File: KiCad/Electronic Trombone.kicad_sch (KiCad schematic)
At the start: 12 parts, among them J1 691137710002, U2 TL074, U3 TL074

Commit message: routed the filter, updated 0201 footprints to 0402
JLCPCB's economy PCBA has a footprint bottom limit of 0402 imperial
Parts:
- R10, R8: footprint Resistor_SMD:R_0201_0603Metric -> Resistor_SMD:R_0402_1005Metric
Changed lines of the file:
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@@
 			)
 		)
-		(property "Footprint" "Resistor_SMD:R_0201_0603Metric"
+		(property "Footprint" "Resistor_SMD:R_0402_1005Metric"
 			(at 131.064 136.144 90)
 			(hide yes)
@@
 			)
 		)
-		(property "Footprint" "Resistor_SMD:R_0201_0603Metric"
+		(property "Footprint" "Resistor_SMD:R_0402_1005Metric"
 			(at 145.034 123.444 90)
 			(hide yes)

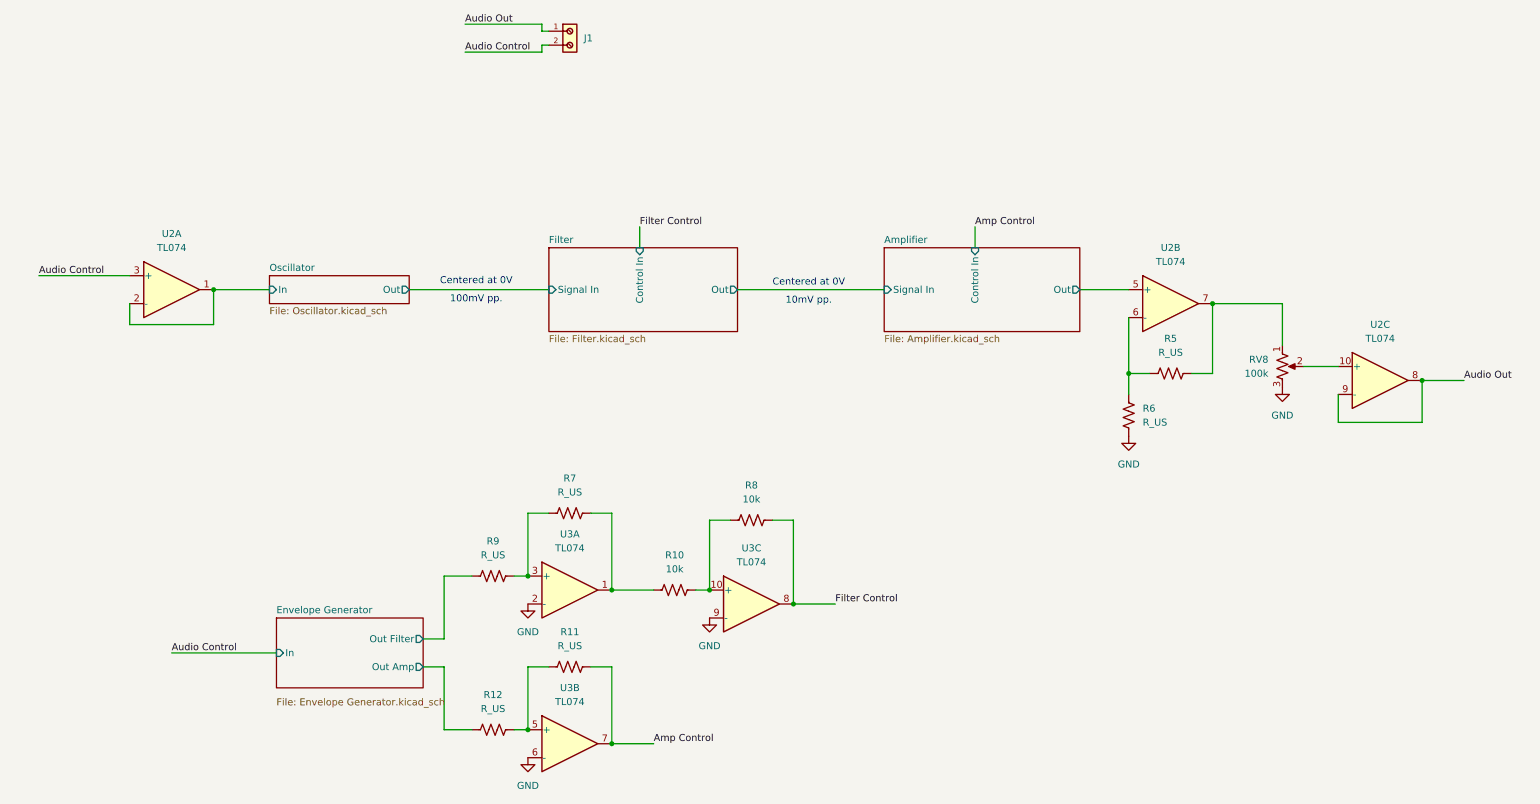
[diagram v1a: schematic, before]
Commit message: amplifier layout and routing
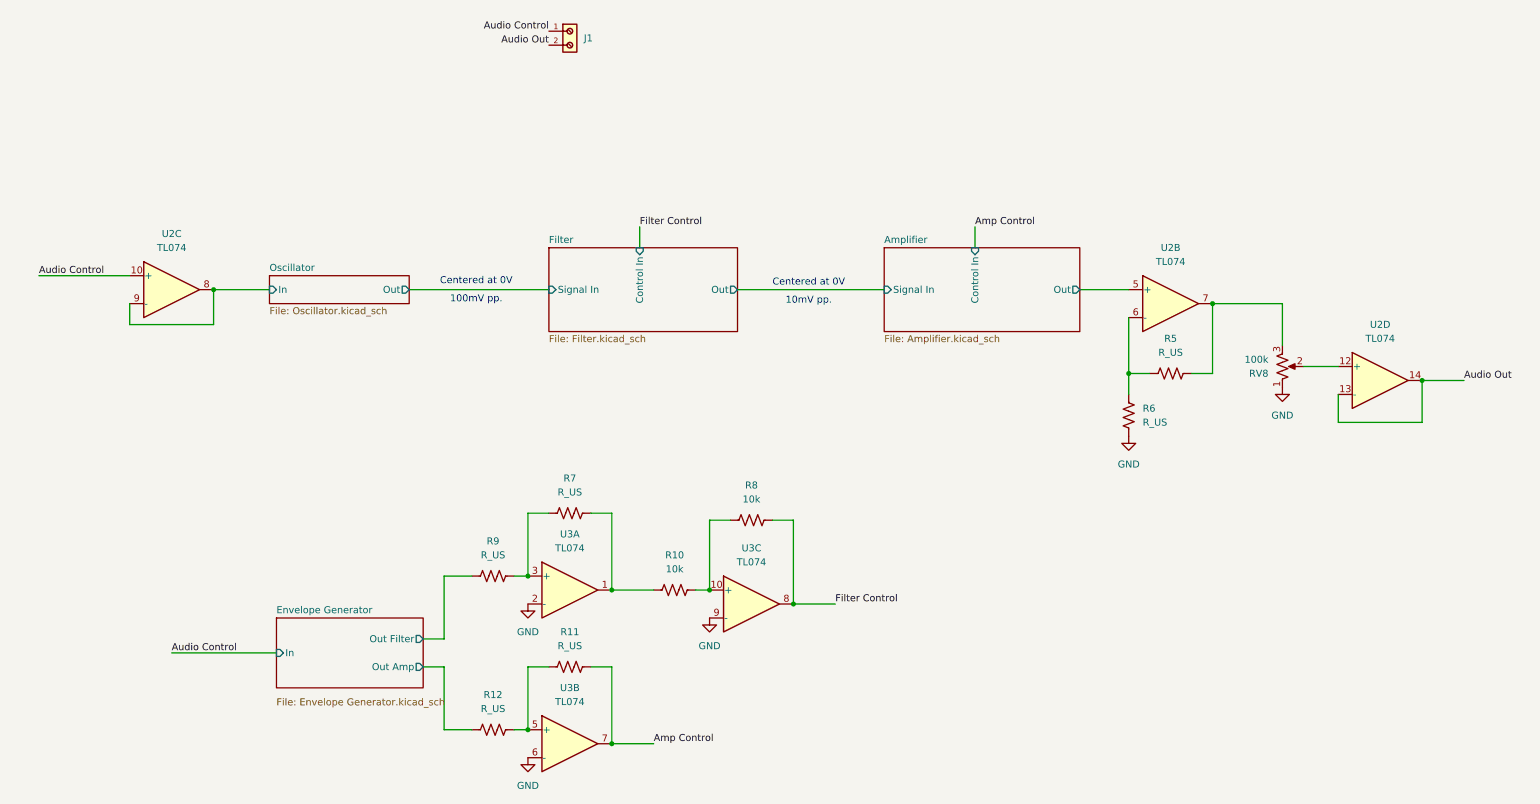
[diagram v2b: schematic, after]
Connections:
- net Audio Control: now also J1.1, U2.10 (+); no longer J1.2, U2.3 (+)
- net Audio Out: now also J1.2, U2.13 (-), U2.14; no longer J1.1, U2.8, U2.9 (-)
- net GND: now also RV8.1; no longer RV8.3
- net Oscillator/In: now also U2.8, U2.9 (-); no longer U2.1, U2.2 (-)
- net at RV8.2: now also U2.12 (+); no longer U2.10 (+)
- net at R5.2, U2.7: now also RV8.3; no longer RV8.1
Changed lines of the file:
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@@
-	(wire
-		(pts
-			(xy 92.71 34.29) (xy 106.68 34.29)
-		)
-		(stroke
-			(width 0)
-			(type default)
-		)
-	)
 	(wire
 		(pts
@@
 	(wire
 		(pts
-			(xy 92.71 39.37) (xy 106.68 39.37)
-		)
-		(stroke
-			(width 0)
-			(type default)
-		)
-	)
-	(wire
-		(pts
 			(xy 217.17 97.79) (xy 213.36 97.79)
 		)
@@
 	(wire
 		(pts
-			(xy 106.68 39.37) (xy 106.68 38.1)
-		)
-		(stroke
-			(width 0)
-			(type default)
-		)
-	)
-	(wire
-		(pts
 			(xy 46.99 88.9) (xy 46.99 82.55)
 		)
@@
 	(wire
 		(pts
-			(xy 106.68 38.1) (xy 107.95 38.1)
-		)
-		(stroke
-			(width 0)
-			(type default)
-		)
-	)
-	(wire
-		(pts
 			(xy 124.46 71.12) (xy 124.46 74.93)
 		)
@@
 	(wire
 		(pts
-			(xy 106.68 34.29) (xy 106.68 35.56)
-		)
-		(stroke
-			(width 0)
-			(type default)
-		)
-	)
-	(wire
-		(pts
 			(xy 107.95 151.13) (xy 104.14 151.13)
 		)
@@
 			(width 0)
 			(type default)
-		)
-	)
-	(wire
-		(pts
-			(xy 106.68 35.56) (xy 107.95 35.56)
-		)
-		(stroke
-			(width 0)
-			(type default)
-		)
-	)
-	(label "Audio Control"
-		(at 92.71 39.37 0)
-		(effects
-			(font
-				(size 1.27 1.27)
-			)
-			(justify left bottom)
 		)
 	)
@@
 	)
 	(label "Audio Out"
-		(at 92.71 34.29 0)
+		(at 107.95 38.1 180)
 		(effects
 			(font
 				(size 1.27 1.27)
 			)
-			(justify left bottom)
+			(justify right bottom)
 		)
 	)
@@
 			)
 			(justify left bottom)
+		)
+	)
+	(label "Audio Control"
+		(at 107.95 35.56 180)
+		(effects
+			(font
+				(size 1.27 1.27)
+			)
+			(justify right bottom)
 		)
 	)
@@
 		(lib_id "Amplifier_Operational:TL074")
 		(at 259.08 99.06 0)
-		(unit 3)
+		(unit 4)
 		(body_style 1)
 		(exclude_from_sim no)
@@
 				(path "/931827f3-33b7-460f-8885-7db258da2648"
 					(reference "U2")
-					(unit 3)
+					(unit 4)
 				)
 			)
@@
 		(lib_id "Device:R_Potentiometer_US")
 		(at 241.3 96.52 0)
+		(mirror x)
 		(unit 1)
 		(body_style 1)
@@
 		(in_pos_files yes)
 		(dnp no)
-		(fields_autoplaced yes)
 		(property "Reference" "RV8"
-			(at 238.76 95.2499 0)
+			(at 238.76 97.7901 0)
 			(show_name no)
 			(do_not_autoplace no)
@@
 		)
 		(property "Value" "100k"
-			(at 238.76 97.7899 0)
+			(at 238.76 95.2501 0)
 			(show_name no)
 			(do_not_autoplace no)
@@
 		(lib_id "Amplifier_Operational:TL074")
 		(at 39.37 82.55 0)
-		(unit 1)
+		(unit 3)
 		(body_style 1)
 		(exclude_from_sim no)
@@
 				(path "/931827f3-33b7-460f-8885-7db258da2648"
 					(reference "U2")
-					(unit 1)
-				)
-			)
+					(unit 3)
+				)
+			)

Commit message: placed and routed envelope core
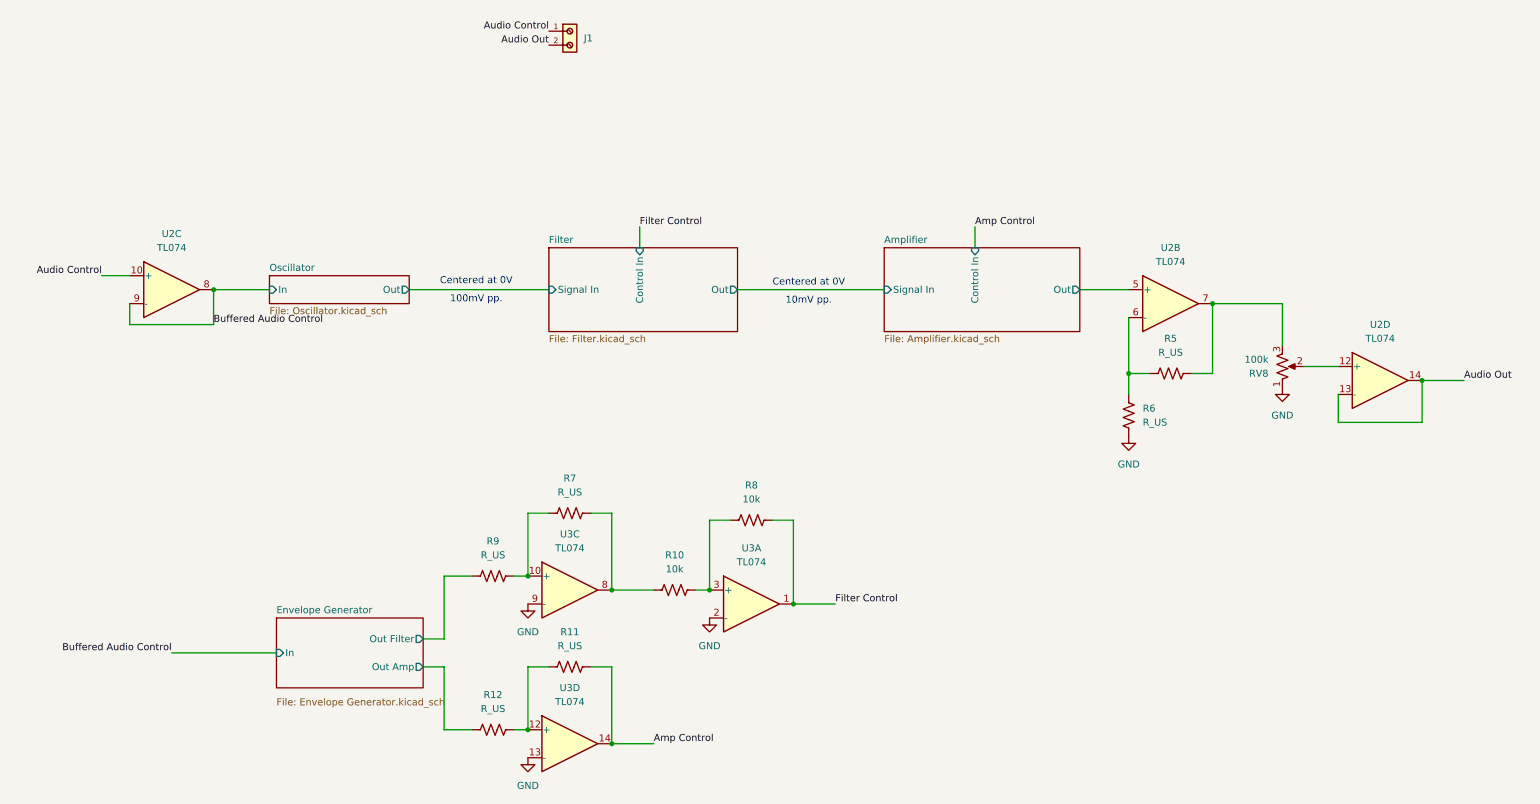
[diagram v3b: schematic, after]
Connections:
- net Amp Control: now also U3.14; no longer U3.7
- net Filter Control: now also U3.1; no longer U3.8
- net GND: now also U3.13 (-), U3.2 (-), U3.9 (-); no longer U3.2 (-), U3.6 (-), U3.9 (-)
- net at R10.2, R8.1: now also U3.3 (+); no longer U3.10 (+)
- net at R10.1, R7.2: now also U3.8; no longer U3.1
- net at R7.1, R9.2: now also U3.10 (+); no longer U3.3 (+)
- net at R11.1, R12.2: now also U3.12 (+); no longer U3.5 (+)
- net Oscillator/In renamed Buffered Audio Control
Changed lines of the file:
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@@
-	(wire
-		(pts
-			(xy 15.24 80.01) (xy 31.75 80.01)
-		)
-		(stroke
-			(width 0)
-			(type default)
-		)
-	)
 	(wire
 		(pts
@@
 	(wire
 		(pts
+			(xy 213.36 82.55) (xy 204.47 82.55)
+		)
+		(stroke
+			(width 0)
+			(type default)
+		)
+	)
+	(wire
+		(pts
+			(xy 115.57 123.19) (xy 119.38 123.19)
+		)
+		(stroke
+			(width 0)
+			(type default)
+		)
+	)
+	(wire
+		(pts
 			(xy 39.37 148.59) (xy 58.42 148.59)
 		)
@@
 	(wire
 		(pts
-			(xy 213.36 82.55) (xy 204.47 82.55)
-		)
-		(stroke
-			(width 0)
-			(type default)
-		)
-	)
-	(wire
-		(pts
-			(xy 115.57 123.19) (xy 119.38 123.19)
-		)
-		(stroke
-			(width 0)
-			(type default)
-		)
-	)
-	(wire
-		(pts
 			(xy 46.99 82.55) (xy 57.15 82.55)
 		)
@@
 	(wire
 		(pts
+			(xy 26.67 80.01) (xy 31.75 80.01)
+		)
+		(stroke
+			(width 0)
+			(type default)
+		)
+	)
+	(wire
+		(pts
 			(xy 241.3 92.71) (xy 241.3 85.09)
 		)
@@
 		)
 	)
-	(label "Audio Control"
-		(at 15.24 80.01 0)
+	(label "Buffered Audio Control"
+		(at 46.99 88.9 0)
 		(effects
 			(font
@@
 			)
 			(justify left bottom)
+		)
+	)
+	(label "Audio Control"
+		(at 26.67 80.01 180)
+		(effects
+			(font
+				(size 1.27 1.27)
+			)
+			(justify right bottom)
 		)
 	)
@@
 		)
 	)
-	(label "Audio Control"
-		(at 39.37 148.59 0)
-		(effects
-			(font
-				(size 1.27 1.27)
-			)
-			(justify left bottom)
-		)
-	)
 	(label "Amp Control"
 		(at 127 165.1 0)
@@
 		)
 	)
+	(label "Buffered Audio Control"
+		(at 39.37 148.59 180)
+		(effects
+			(font
+				(size 1.27 1.27)
+			)
+			(justify right bottom)
+		)
+	)
 	(label "Audio Out"
 		(at 274.32 99.06 0)
@@
 		(lib_id "Amplifier_Operational:TL074")
 		(at 144.78 139.7 0)
-		(unit 3)
+		(unit 1)
 		(body_style 1)
 		(exclude_from_sim no)
@@
 				(path "/931827f3-33b7-460f-8885-7db258da2648"
 					(reference "U3")
-					(unit 3)
+					(unit 1)
 				)
 			)
@@
 		(lib_id "Amplifier_Operational:TL074")
 		(at 111.76 137.16 0)
-		(unit 1)
+		(unit 3)
 		(body_style 1)
 		(exclude_from_sim no)
@@
 				(path "/931827f3-33b7-460f-8885-7db258da2648"
 					(reference "U3")
-					(unit 1)
+					(unit 3)
 				)
 			)
@@
 		(lib_id "Amplifier_Operational:TL074")
 		(at 111.76 165.1 0)
-		(unit 2)
+		(unit 4)
 		(body_style 1)
 		(exclude_from_sim no)
@@
 				(path "/931827f3-33b7-460f-8885-7db258da2648"
 					(reference "U3")
-					(unit 2)
-				)
-			)
+					(unit 4)
+				)
+			)

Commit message: routed rest of the envelope generator
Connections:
- net GND: now also U3.6 (-); no longer U3.9 (-)
- net at R7.1, R9.2: now also U3.5 (+); no longer U3.10 (+)
- net at R10.1, R7.2: now also U3.7; no longer U3.8
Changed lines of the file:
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@@
 		(lib_id "Amplifier_Operational:TL074")
 		(at 111.76 137.16 0)
-		(unit 3)
+		(unit 2)
 		(body_style 1)
 		(exclude_from_sim no)
@@
 				(path "/931827f3-33b7-460f-8885-7db258da2648"
 					(reference "U3")
-					(unit 3)
+					(unit 2)
 				)
 			)

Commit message: second checkpoint before complete redo of pcb
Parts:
- R10: footprint Resistor_SMD:R_0402_1005Metric -> Resistor_THT:R_Axial_DIN0207_L6.3mm_D2.5mm_P7.62mm_Horizontal
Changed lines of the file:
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@@
 			)
 		)
-		(property "Footprint" "Resistor_SMD:R_0402_1005Metric"
+		(property "Footprint" "Resistor_THT:R_Axial_DIN0207_L6.3mm_D2.5mm_P7.62mm_Horizontal"
 			(at 131.064 136.144 90)
 			(hide yes)

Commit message: Revert "second checkpoint before complete redo of pcb"
This reverts commit 4d5d4d4b5e4cbbcaee48991b351946aeae31b1e5.
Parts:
- R10: footprint Resistor_THT:R_Axial_DIN0207_L6.3mm_D2.5mm_P7.62mm_Horizontal -> Resistor_SMD:R_0402_1005Metric
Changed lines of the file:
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@@
 			)
 		)
-		(property "Footprint" "Resistor_THT:R_Axial_DIN0207_L6.3mm_D2.5mm_P7.62mm_Horizontal"
+		(property "Footprint" "Resistor_SMD:R_0402_1005Metric"
 			(at 131.064 136.144 90)
 			(hide yes)

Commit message: all SMD are 0603 (imperial) now, started rerouting all traces
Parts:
- R10, R8: footprint Resistor_SMD:R_0402_1005Metric -> Resistor_SMD:R_0603_1608Metric
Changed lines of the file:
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@@
+			)
+		)
+		(property "LCSC Part #" ""
+			(at 144.78 139.7 0)
+			(hide yes)
+			(show_name no)
+			(do_not_autoplace no)
+			(effects
+				(font
+					(size 1.27 1.27)
+				)
 			)
 		)
@@
 			)
 		)
+		(property "LCSC Part #" ""
+			(at 259.08 99.06 0)
+			(hide yes)
+			(show_name no)
+			(do_not_autoplace no)
+			(effects
+				(font
+					(size 1.27 1.27)
+				)
+			)
+		)
 		(pin "13"
 		)
@@
 			)
 		)
+		(property "LCSC Part #" ""
+			(at 113.03 38.1 90)
+			(hide yes)
+			(show_name no)
+			(do_not_autoplace no)
+			(effects
+				(font
+					(size 1.27 1.27)
+				)
+			)
+		)
 		(pin "1"
 		)
@@
 			)
 		)
+		(property "LCSC Part #" ""
+			(at 111.76 137.16 0)
+			(hide yes)
+			(show_name no)
+			(do_not_autoplace no)
+			(effects
+				(font
+					(size 1.27 1.27)
+				)
+			)
+		)
 		(pin "2"
 		)
@@
 			)
 		)
+		(property "LCSC Part #" ""
+			(at 111.76 123.19 90)
+			(hide yes)
+			(show_name no)
+			(do_not_autoplace no)
+			(effects
+				(font
+					(size 1.27 1.27)
+				)
+			)
+		)
 		(pin "1"
 		)
@@
 			)
 		)
+		(property "LCSC Part #" ""
+			(at 97.79 134.62 90)
+			(hide yes)
+			(show_name no)
+			(do_not_autoplace no)
+			(effects
+				(font
+					(size 1.27 1.27)
+				)
+			)
+		)
 		(pin "1"
 		)
@@
 			)
 		)
+		(property "LCSC Part #" ""
+			(at 241.3 96.52 0)
+			(hide yes)
+			(show_name no)
+			(do_not_autoplace no)
+			(effects
+				(font
+					(size 1.27 1.27)
+				)
+			)
+		)
 		(pin "1"
 		)
@@
 			)
 		)
+		(property "LCSC Part #" ""
+			(at 39.37 82.55 0)
+			(hide yes)
+			(show_name no)
+			(do_not_autoplace no)
+			(effects
+				(font
+					(size 1.27 1.27)
+				)
+			)
+		)
 		(pin "13"
 		)
@@
 			)
 		)
-		(property "Footprint" "Resistor_SMD:R_0402_1005Metric"
+		(property "Footprint" "Resistor_SMD:R_0603_1608Metric"
 			(at 131.064 136.144 90)
 			(hide yes)
@@
 		(property "Description" "Resistor, US symbol"
 			(at 130.81 137.16 0)
+			(hide yes)
+			(show_name no)
+			(do_not_autoplace no)
+			(effects
+				(font
+					(size 1.27 1.27)
+				)
+			)
+		)
+		(property "LCSC Part #" ""
+			(at 130.81 137.16 90)
 			(hide yes)
 			(show_name no)
@@
 			)
 		)
+		(property "LCSC Part #" ""
+			(at 111.76 165.1 0)
+			(hide yes)
+			(show_name no)
+			(do_not_autoplace no)
+			(effects
+				(font
+					(size 1.27 1.27)
+				)
+			)
+		)
 		(pin "2"
 		)
@@
 			)
 		)
+		(property "LCSC Part #" ""
+			(at 97.79 162.56 90)
+			(hide yes)
+			(show_name no)
+			(do_not_autoplace no)
+			(effects
+				(font
+					(size 1.27 1.27)
+				)
+			)
+		)
 		(pin "1"
 		)
@@
 			)
 		)
+		(property "LCSC Part #" ""
+			(at 220.98 97.79 90)
+			(hide yes)
+			(show_name no)
+			(do_not_autoplace no)
+			(effects
+				(font
+					(size 1.27 1.27)
+				)
+			)
+		)
 		(pin "1"
 		)
@@
 			)
 		)
-		(property "Footprint" "Resistor_SMD:R_0402_1005Metric"
+		(property "Footprint" "Resistor_SMD:R_0603_1608Metric"
 			(at 145.034 123.444 90)
 			(hide yes)
@@
 		(property "Description" "Resistor, US symbol"
 			(at 144.78 124.46 0)
+			(hide yes)
+			(show_name no)
+			(do_not_autoplace no)
+			(effects
+				(font
+					(size 1.27 1.27)
+				)
+			)
+		)
+		(property "LCSC Part #" ""
+			(at 144.78 124.46 90)
 			(hide yes)
 			(show_name no)
@@
 			)
 		)
+		(property "LCSC Part #" ""
+			(at 111.76 151.13 90)
+			(hide yes)
+			(show_name no)
+			(do_not_autoplace no)
+			(effects
+				(font
+					(size 1.27 1.27)
+				)
+			)
+		)
 		(pin "1"
 		)
@@
 			)
 		)
+		(property "LCSC Part #" ""
+			(at 213.36 105.41 0)
+			(hide yes)
+			(show_name no)
+			(do_not_autoplace no)
+			(effects
+				(font
+					(size 1.27 1.27)
+				)
+			)
+		)
 		(pin "1"
 		)
@@
 			(at 220.98 85.09 0)
 			(hide yes)
+			(show_name no)
+			(do_not_autoplace no)
+			(effects
+				(font
+					(size 1.27 1.27)
+				)
+			)
+		)
+		(property "LCSC Part #" ""
+			(at 220.98 85.09 0)
+			(hide yes)

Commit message: first JLCPCB order
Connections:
- net Amplifier/Out: now also U2.3 (+); no longer U2.5 (+)
- net at R5.2, RV8.3: now also U2.1; no longer U2.7
- net at R5.1, R6.2: now also U2.2 (-); no longer U2.6 (-)
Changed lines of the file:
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@@
 		(lib_id "Amplifier_Operational:TL074")
 		(at 220.98 85.09 0)
-		(unit 2)
+		(unit 1)
 		(body_style 1)
 		(exclude_from_sim no)
@@
 				(path "/931827f3-33b7-460f-8885-7db258da2648"
 					(reference "U2")
-					(unit 2)
+					(unit 1)
 				)
 			)
